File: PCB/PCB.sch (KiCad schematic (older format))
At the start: 96 parts, among them J1 Conn, J2 Conn, Q1 Q_NPN_BCE, Q10 Q_NPN, Q11 Q_PNP_BCE, Q12 Q_NPN, Q13 Q_PNP, Q14 Q_PNP_BCE, Q15 Q_PNP_BCE, Q16 Q-NPN, Q17 Q-NPN, Q18 Q-NPN, Q19 Q-PNP, Q2 Q_PNP_BCE, Q20 Q-NPN, Q21 Q-PNP, Q22 Q-NPN, Q23 Q-PNP, Q24 Q-PNP, Q25 Q-NPN, Q26 Q-NPN, Q27 Q-PNP, Q28 Q-NPN, Q29 Q_PNP, Q3 Q_NPN_BCE, Q4 Q_PNP_BCE, Q5 Q_NPN_BCE, Q6 Q_PNP_BCE, Q7 Q_PNP_BCE, Q8 Q_NPN_BCE, Q9 Q_NPN_BCE

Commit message: Etapa salida PCB cheta
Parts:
- D11, D12: footprint Diodes_SMD:D_SOT-23_ANK -> Diode_SMD:D_SOT-23_ANK
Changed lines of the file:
@@
 F 0 "D12" V 9246 1371 50  0000 R CNN
 F 1 "D_Sch" V 9155 1371 50  0000 R CNN
-F 2 "Diodes_SMD:D_SOT-23_ANK" H 9200 1450 50  0001 C CNN
+F 2 "Diode_SMD:D_SOT-23_ANK" H 9200 1450 50  0001 C CNN
 F 3 "~" H 9200 1450 50  0001 C CNN
 	1    9200 1450
@@
 F 0 "D11" V 9196 5471 50  0000 R CNN
 F 1 "D_Sch" V 9105 5471 50  0000 R CNN
-F 2 "Diodes_SMD:D_SOT-23_ANK" H 9150 5550 50  0001 C CNN
+F 2 "Diode_SMD:D_SOT-23_ANK" H 9150 5550 50  0001 C CNN
 F 3 "~" H 9150 5550 50  0001 C CNN
 	1    9150 5550

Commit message: pcb update
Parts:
- added J3, J4: Conn_01x02_Female, Connector:JWT_A3963_1x02_P3.96mm_Vertical, symbol Connector:Conn_01x02_Female
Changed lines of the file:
@@
 	950  4650 950  5150
 Wire Wire Line
-	950  5150 1300 5150
+	950  5150 1200 5150
 Connection ~ 1300 5150
 Wire Wire Line
@@
 Wire Wire Line
 	7200 4750 7200 4950
+$Comp
+L Connector:Conn_01x02_Female J3
+U 1 1 5D3536FE
+P 950 850
+F 0 "J3" H 978 826 50  0000 L CNN
+F 1 "Conn_01x02_Female" H 978 735 50  0000 L CNN
+F 2 "Connector:JWT_A3963_1x02_P3.96mm_Vertical" H 950 850 50  0001 C CNN
+F 3 "~" H 950 850 50  0001 C CNN
+	1    950  850
+	1    0    0    -1
+$EndComp
+Wire Wire Line
+	950  850  950  750
+Wire Wire Line
+	950  750  1650 750
+Connection ~ 1650 750
+Wire Wire Line
+	950  950  1050 950
+Wire Wire Line
+	1050 950  1050 4250
+Wire Wire Line
+	1050 4250 850  4250
+Wire Wire Line
+	850  4250 850  5150
+Wire Wire Line
+	850  5150 950  5150
+Connection ~ 950  5150
+$Comp
+L Connector:Conn_01x02_Female J4
+U 1 1 5D375B30
+P 1000 7050
+F 0 "J4" H 1028 7026 50  0000 L CNN
+F 1 "Conn_01x02_Female" H 1028 6935 50  0000 L CNN
+F 2 "Connector:JWT_A3963_1x02_P3.96mm_Vertical" H 1000 7050 50  0001 C CNN
+F 3 "~" H 1000 7050 50  0001 C CNN
+	1    1000 7050
+	1    0    0    -1
+$EndComp
+Wire Wire Line
+	1000 7050 1200 7050
+Wire Wire Line
+	1200 7050 1200 5150
+Connection ~ 1200 5150
+Wire Wire Line
+	1200 5150 1300 5150
+Wire Wire Line
+	1000 7150 2250 7150
+Wire Wire Line
+	2250 7150 2250 7050
+Connection ~ 2250 7050
 $EndSCHEMATC

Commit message: pcb v1.0
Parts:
- removed J3, J4: Conn_01x02_Female, Connector:JWT_A3963_1x02_P3.96mm_Vertical, symbol Connector:Conn_01x02_Female
- added J3, J4, J5, J6: Screw_Terminal_01x02, Connector:JWT_A3963_1x02_P3.96mm_Vertical, symbol Connector:Screw_Terminal_01x02
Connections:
- net +15V: now also J6.1 (Pin_1)
- net -15V: now also J5.2 (Pin_2)
- net GND: now also J3.1 (Pin_1), J4.2 (Pin_2), J5.1 (Pin_1), J6.2 (Pin_2)
- net VCC: now also J3.2 (Pin_2)
- net VEE: now also J4.1 (Pin_1)
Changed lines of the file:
@@
 $EndComp
 Wire Wire Line
-	10350 3600 10350 3700
+	10350 3600 10350 3650
 $Comp
 L Device:Q_NPN_BCE Q16
@@
 $EndComp
 Wire Wire Line
-	10550 5100 9450 5100
+	10550 5100 10450 5100
 $Comp
 L power:GND #PWR0110
@@
 Wire Wire Line
 	7200 4750 7200 4950
-$Comp
-L Connector:Conn_01x02_Female J3
-U 1 1 5D3536FE
-P 950 850
-F 0 "J3" H 978 826 50  0000 L CNN
-F 1 "Conn_01x02_Female" H 978 735 50  0000 L CNN
-F 2 "Connector:JWT_A3963_1x02_P3.96mm_Vertical" H 950 850 50  0001 C CNN
-F 3 "~" H 950 850 50  0001 C CNN
-	1    950  850
-	1    0    0    -1
-$EndComp
 Wire Wire Line
 	950  850  950  750
@@
 Connection ~ 1650 750
 Wire Wire Line
-	950  950  1050 950
-Wire Wire Line
 	1050 950  1050 4250
 Wire Wire Line
@@
 	850  5150 950  5150
 Connection ~ 950  5150
-$Comp
-L Connector:Conn_01x02_Female J4
-U 1 1 5D375B30
-P 1000 7050
-F 0 "J4" H 1028 7026 50  0000 L CNN
-F 1 "Conn_01x02_Female" H 1028 6935 50  0000 L CNN
-F 2 "Connector:JWT_A3963_1x02_P3.96mm_Vertical" H 1000 7050 50  0001 C CNN
-F 3 "~" H 1000 7050 50  0001 C CNN
-	1    1000 7050
-	1    0    0    -1
-$EndComp
-Wire Wire Line
-	1000 7050 1200 7050
 Wire Wire Line
 	1200 7050 1200 5150
@@
 	1200 5150 1300 5150
 Wire Wire Line
-	1000 7150 2250 7150
-Wire Wire Line
 	2250 7150 2250 7050
 Connection ~ 2250 7050
+$Comp
+L Connector:Screw_Terminal_01x02 J4
+U 1 1 5D35D2AD
+P 700 7150
+F 0 "J4" H 618 6825 50  0000 C CNN
+F 1 "Screw_Terminal_01x02" H 618 6916 50  0000 C CNN
+F 2 "Connector:JWT_A3963_1x02_P3.96mm_Vertical" H 700 7150 50  0001 C CNN
+F 3 "~" H 700 7150 50  0001 C CNN
+	1    700  7150
+	-1   0    0    1
+$EndComp
+Wire Wire Line
+	900  7050 1200 7050
+Wire Wire Line
+	900  7150 2250 7150
+$Comp
+L Connector:Screw_Terminal_01x02 J3
+U 1 1 5D3A1EE3
+P 600 950
+F 0 "J3" H 518 625 50  0000 C CNN
+F 1 "Screw_Terminal_01x02" H 518 716 50  0000 C CNN
+F 2 "Connector:JWT_A3963_1x02_P3.96mm_Vertical" H 600 950 50  0001 C CNN
+F 3 "~" H 600 950 50  0001 C CNN
+	1    600  950
+	-1   0    0    1
+$EndComp
+Wire Wire Line
+	950  850  800  850
+Wire Wire Line
+	800  950  1050 950
+$Comp
+L Connector:Screw_Terminal_01x02 J5
+U 1 1 5D3DCE43
+P 10850 5100
+F 0 "J5" H 10930 5092 50  0000 L CNN
+F 1 "Screw_Terminal_01x02" H 10930 5001 50  0000 L CNN
+F 2 "Connector:JWT_A3963_1x02_P3.96mm_Vertical" H 10850 5100 50  0001 C CNN
+F 3 "~" H 10850 5100 50  0001 C CNN
+	1    10850 5100
+	1    0    0    -1
+$EndComp
+$Comp
+L Connector:Screw_Terminal_01x02 J6
+U 1 1 5D3DDFAC
+P 10900 1850
+F 0 "J6" H 10980 1842 50  0000 L CNN
+F 1 "Screw_Terminal_01x02" H 10980 1751 50  0000 L CNN
+F 2 "Connector:JWT_A3963_1x02_P3.96mm_Vertical" H 10900 1850 50  0001 C CNN
+F 3 "~" H 10900 1850 50  0001 C CNN
+	1    10900 1850
+	1    0    0    -1
+$EndComp
+Wire Wire Line
+	10550 1850 10700 1850
+Connection ~ 10550 1850
+Wire Wire Line
+	10700 1950 10600 1950
+Wire Wire Line
+	10600 3150 10800 3150
+Wire Wire Line
+	10800 3150 10800 3650
+Wire Wire Line
+	10600 1950 10600 3150
+Connection ~ 10350 3650
+Wire Wire Line
+	10350 3650 10350 3700
+Wire Wire Line
+	10650 5200 10450 5200
+Wire Wire Line
+	10450 5200 10450 5100
+Connection ~ 10450 5100
+Wire Wire Line
+	10450 5100 9450 5100
+Wire Wire Line
+	10650 5100 10650 3650
+Wire Wire Line
+	10350 3650 10650 3650
+Connection ~ 10650 3650
+Wire Wire Line
+	10650 3650 10800 3650
 $EndSCHEMATC

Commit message: update pcb
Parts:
- J1: footprint Connectors:PJ320D_3.5mm_Jack -> Connector:PJ320D_3.5mm_Jack
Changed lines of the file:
@@
 F 0 "J1" H 492 4735 50  0000 C CNN
 F 1 "Conn" H 492 4644 50  0000 C CNN
-F 2 "Connectors:PJ320D_3.5mm_Jack" H 600 4550 50  0001 C CNN
+F 2 "Connector:PJ320D_3.5mm_Jack" H 600 4550 50  0001 C CNN
 F 3 "~" H 600 4550 50  0001 C CNN
 	1    600  4550

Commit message: update
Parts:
- removed J1: Conn, Connector:PJ320D_3.5mm_Jack, symbol Connector:Conn_01x02_Female
- added J1, J7: Conn_01x01_MountingPin, symbol Connector_Generic_MountingPin:Conn_01x01_MountingPin
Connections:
- net GND: now also J7.1 (Pin_1); no longer J5.1 (Pin_1)
- net at C1.1: now also J1.MP (MountPin)
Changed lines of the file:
@@
 	3250 6350 3250 6550
-$Comp
-L Connector:Conn_01x02_Female J1
-U 1 1 5D1D8FF0
-P 600 4550
-F 0 "J1" H 492 4735 50  0000 C CNN
-F 1 "Conn" H 492 4644 50  0000 C CNN
-F 2 "Connector:PJ320D_3.5mm_Jack" H 600 4550 50  0001 C CNN
-F 3 "~" H 600 4550 50  0001 C CNN
-	1    600  4550
-	-1   0    0    -1
-$EndComp
-Wire Wire Line
-	800  4550 950  4550
-Wire Wire Line
-	950  4650 800  4650
 $Comp
 L Device:R R43
@@
 	10450 5100 9450 5100
 Wire Wire Line
-	10650 5100 10650 3650
+	-1300 5950 -1300 4500
 Wire Wire Line
-	10350 3650 10650 3650
-Connection ~ 10650 3650
+	10350 3650 10800 3650
 Wire Wire Line
-	10650 3650 10800 3650
+	950  4650 750  4650
+Wire Wire Line
+	950  4550 750  4550
+$Comp
+L Connector_Generic_MountingPin:Conn_01x01_MountingPin J1
+U 1 1 5D48F635
+P 750 4350
+F 0 "J1" H 838 4314 50  0000 L CNN
+F 1 "Conn_01x01_MountingPin" H 838 4223 50  0000 L CNN
+F 2 "" H 750 4350 50  0001 C CNN
+F 3 "~" H 750 4350 50  0001 C CNN
+	1    750  4350
+	1    0    0    -1
+$EndComp
+Connection ~ 750  4550
+Wire Wire Line
+	750  4550 650  4550
+$Comp
+L Connector_Generic_MountingPin:Conn_01x01_MountingPin J7
+U 1 1 5D491977
+P 750 4850
+F 0 "J7" V 626 4930 50  0000 L CNN
+F 1 "Conn_01x01_MountingPin" V 717 4930 50  0000 L CNN
+F 2 "" H 750 4850 50  0001 C CNN
+F 3 "~" H 750 4850 50  0001 C CNN
+	1    750  4850
+	0    1    1    0
+$EndComp
+Connection ~ 750  4650
+Wire Wire Line
+	750  4650 650  4650
 $EndSCHEMATC

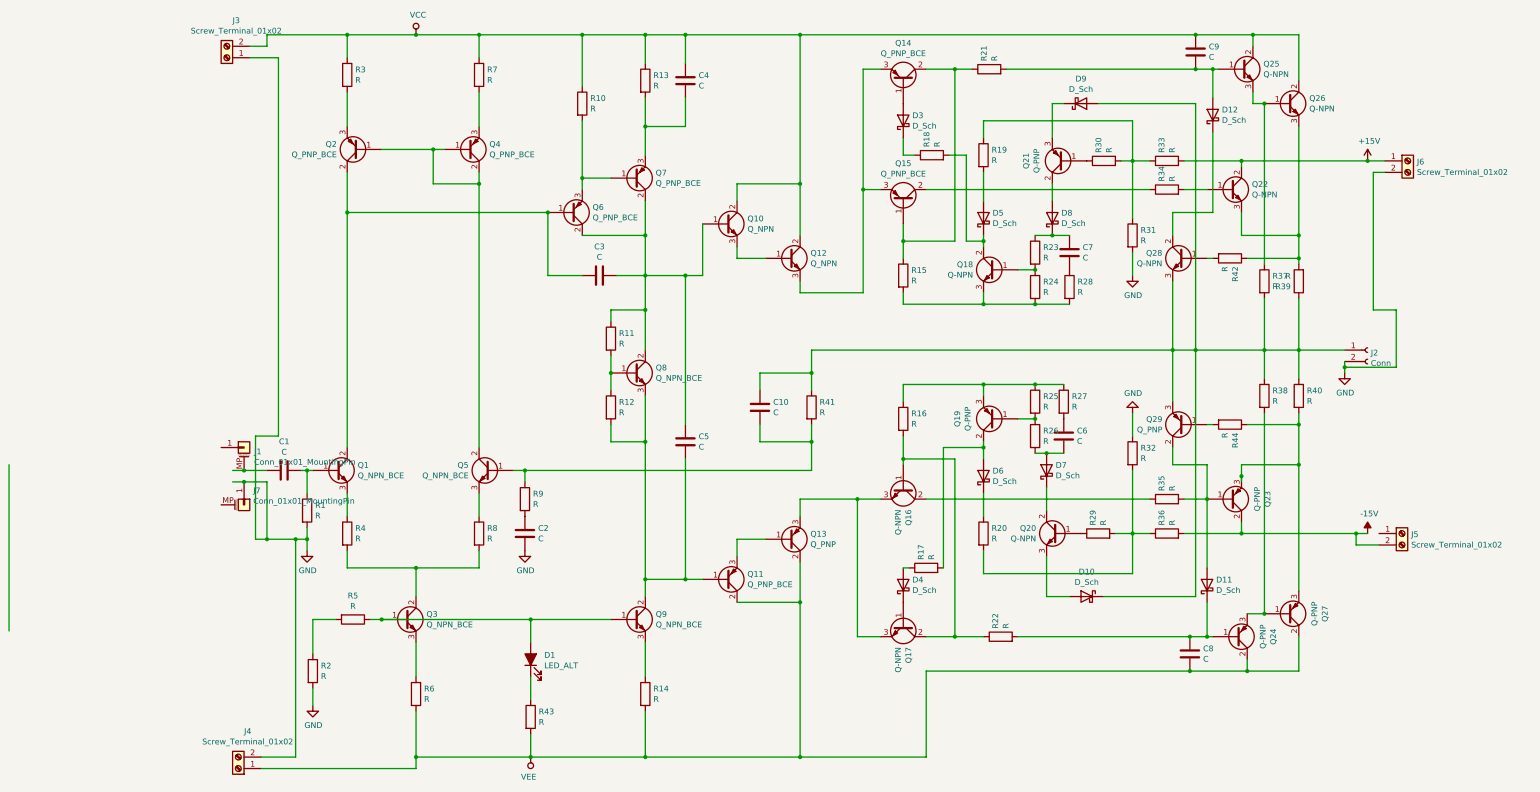
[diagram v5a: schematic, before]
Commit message: Agregados los capacitores de alimentacion, pistas a las borneras sobre cara superior y a capacitores por cara inferior. Faltaría acomodar los FILL
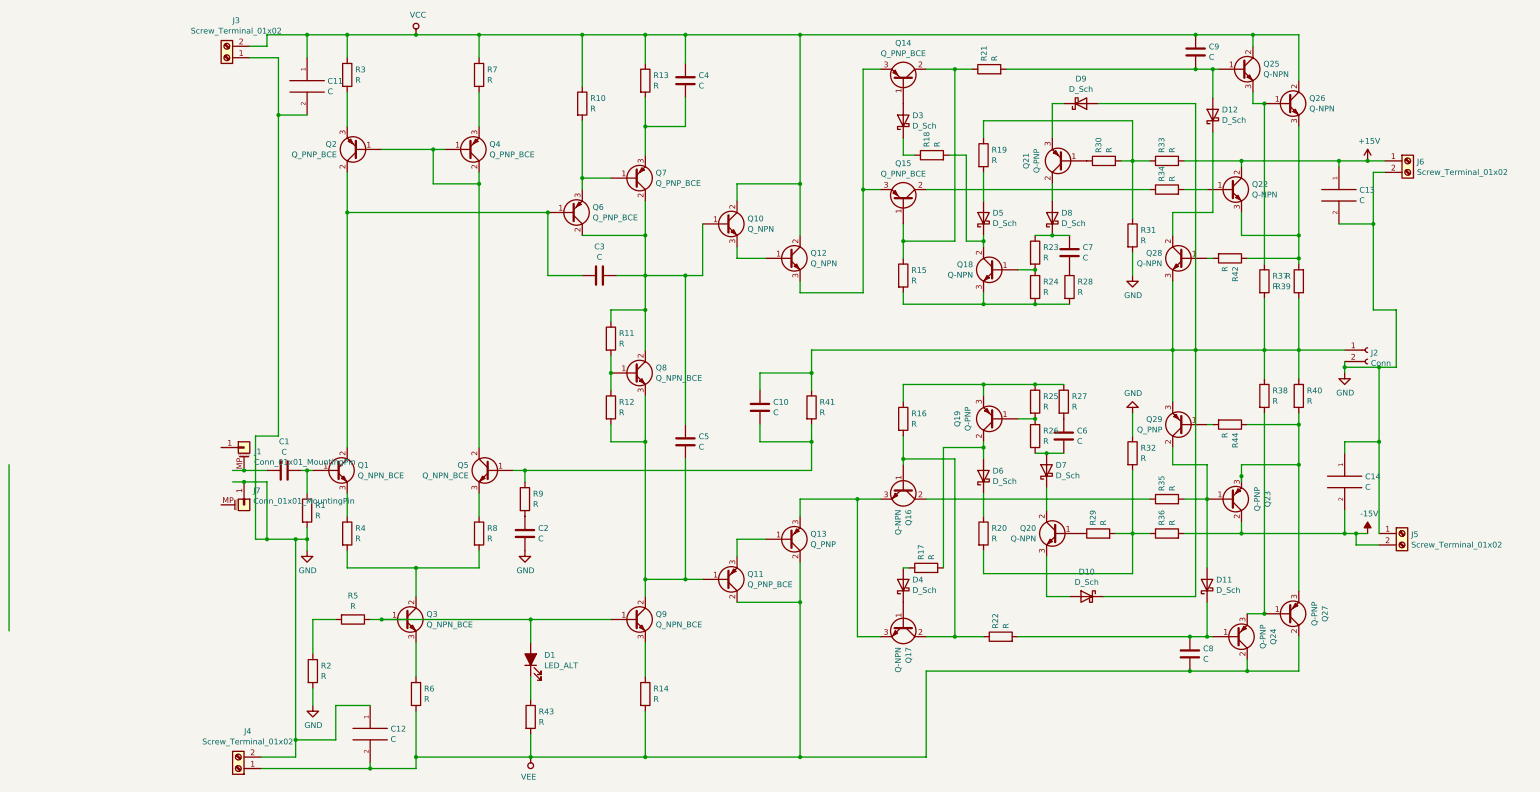
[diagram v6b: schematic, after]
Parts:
- added C11, C12, C13, C14: C, Capacitor_THT:C_Radial_D12.5mm_H20.0mm_P5.00mm, symbol pspice:C
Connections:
- net +15V: now also C13.1
- net -15V: now also C14.2
- net GND: now also J5.1 (Pin_1), C11.2, C12.1, C13.2, C14.1
- net VCC: now also C11.1
- net VEE: now also C12.2
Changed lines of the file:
@@
 EESchema Schematic File Version 4
 LIBS:PCB-cache
-EELAYER 29 0
+EELAYER 30 0
 EELAYER END
 $Descr A4 11693 8268
@@
 Connection ~ 9450 1850
 Wire Wire Line
-	9450 1850 10550 1850
+	9450 1850 10300 1850
 Wire Wire Line
 	9150 2100 8950 2100
@@
 	950  850  950  750
 Wire Wire Line
-	950  750  1650 750
+	950  750  1300 750
 Connection ~ 1650 750
 Wire Wire Line
-	1050 950  1050 4250
+	1050 950  1050 1450
 Wire Wire Line
 	1050 4250 850  4250
@@
 	850  5150 950  5150
 Connection ~ 950  5150
-Wire Wire Line
-	1200 7050 1200 5150
 Connection ~ 1200 5150
 Wire Wire Line
@@
 	900  7050 1200 7050
 Wire Wire Line
-	900  7150 2250 7150
+	900  7150 1850 7150
 $Comp
 L Connector:Screw_Terminal_01x02 J3
@@
 	10800 3150 10800 3650
 Wire Wire Line
-	10600 1950 10600 3150
+	10600 1950 10600 2400
 Connection ~ 10350 3650
 Wire Wire Line
@@
 Connection ~ 10450 5100
 Wire Wire Line
-	10450 5100 9450 5100
+	10450 5100 10350 5100
 Wire Wire Line
 	-1300 5950 -1300 4500
 Wire Wire Line
-	10350 3650 10800 3650
+	10350 3650 10650 3650
 Wire Wire Line
 	950  4650 750  4650
@@
 Wire Wire Line
 	750  4650 650  4650
+$Comp
+L pspice:C C13
+U 1 1 5D93BB79
+P 10300 2150
+F 0 "C13" H 10478 2196 50  0000 L CNN
+F 1 "C" H 10478 2105 50  0000 L CNN
+F 2 "Capacitor_THT:C_Radial_D12.5mm_H20.0mm_P5.00mm" H 10300 2150 50  0001 C CNN
+F 3 "~" H 10300 2150 50  0001 C CNN
+	1    10300 2150
+	1    0    0    -1
+$EndComp
+$Comp
+L pspice:C C14
+U 1 1 5D93ED6D
+P 10350 4650
+F 0 "C14" H 10528 4696 50  0000 L CNN
+F 1 "C" H 10528 4605 50  0000 L CNN
+F 2 "Capacitor_THT:C_Radial_D12.5mm_H20.0mm_P5.00mm" H 10350 4650 50  0001 C CNN
+F 3 "~" H 10350 4650 50  0001 C CNN
+	1    10350 4650
+	1    0    0    -1
+$EndComp
+$Comp
+L pspice:C C12
+U 1 1 5D940FAA
+P 1850 6850
+F 0 "C12" H 2028 6896 50  0000 L CNN
+F 1 "C" H 2028 6805 50  0000 L CNN
+F 2 "Capacitor_THT:C_Radial_D12.5mm_H20.0mm_P5.00mm" H 1850 6850 50  0001 C CNN
+F 3 "~" H 1850 6850 50  0001 C CNN
+	1    1850 6850
+	1    0    0    -1
+$EndComp
+$Comp
+L pspice:C C11
+U 1 1 5D941CAC
+P 1300 1200
+F 0 "C11" H 1478 1246 50  0000 L CNN
+F 1 "C" H 1478 1155 50  0000 L CNN
+F 2 "Capacitor_THT:C_Radial_D12.5mm_H20.0mm_P5.00mm" H 1300 1200 50  0001 C CNN
+F 3 "~" H 1300 1200 50  0001 C CNN
+	1    1300 1200
+	1    0    0    -1
+$EndComp
+Wire Wire Line
+	1300 950  1300 750
+Connection ~ 1300 750
+Wire Wire Line
+	1300 750  1650 750
+Wire Wire Line
+	1300 1450 1050 1450
+Connection ~ 1050 1450
+Wire Wire Line
+	1050 1450 1050 4250
+Wire Wire Line
+	1850 7100 1850 7150
+Connection ~ 1850 7150
+Wire Wire Line
+	1850 7150 2250 7150
+Wire Wire Line
+	1850 6600 1550 6600
+Wire Wire Line
+	1550 6600 1550 6900
+Wire Wire Line
+	1550 6900 1200 6900
+Wire Wire Line
+	1200 5150 1200 6900
+Connection ~ 1200 6900
+Wire Wire Line
+	1200 6900 1200 7050
+Wire Wire Line
+	10650 5100 10650 4300
+Connection ~ 10650 3650
+Wire Wire Line
+	10650 3650 10800 3650
+Wire Wire Line
+	10350 4900 10350 5100
+Connection ~ 10350 5100
+Wire Wire Line
+	10350 5100 9450 5100
+Wire Wire Line
+	10350 4400 10350 4300
+Wire Wire Line
+	10350 4300 10650 4300
+Connection ~ 10650 4300
+Wire Wire Line
+	10650 4300 10650 3650
+Wire Wire Line
+	10300 1900 10300 1850
+Connection ~ 10300 1850
+Wire Wire Line
+	10300 1850 10550 1850
+Wire Wire Line
+	10300 2400 10600 2400
+Connection ~ 10600 2400
+Wire Wire Line
+	10600 2400 10600 3150
 $EndSCHEMATC
